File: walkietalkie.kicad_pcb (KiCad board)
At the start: 2 copper layers, 51.2 x 89.7 mm, 13 parts, among them J1 Conn_01x05_Pin, J2 Conn_01x02_Pin, J3 Conn_01x02_Pin, SW1 PTT, U2 NRF24L01_Breakout, U7 ER_OLEDM0.91_1x-I2C

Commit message: routing done
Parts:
- removed REF**: TestPoint_Pad_D1.0mm, TestPoint:TestPoint_Pad_D1.0mm
- added C1: C_Polarized, Capacitor_THT:CP_Radial_D8.0mm_P3.80mm, B.Cu at (133.0, 95.7)
- added R1: R, Resistor_THT:R_Axial_DIN0207_L6.3mm_D2.5mm_P10.16mm_Horizontal, F.Cu at (164.1, 76.0)
- added U6: SK12D07VG4, pcbcupidd_footprint:SK12D07VG4, B.Cu at (159.2, 147.2)
- D1: value LED_KRGB -> LED; footprint LED_THT:LED_D5.0mm-4_RGB -> LED_THT:LED_D5.0mm
- moved J2 24.3 mm to (150.1, 97.9)
- moved J3 24.3 mm to (156.1, 100.4)
- moved D1 2.83 mm to (159.3, 63.5)
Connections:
- BT1 pad 1: (no net) -> Net-(BT1-Pad1)
- BT1 pad 2: (no net) -> GND
- D1 pad 1: unconnected-(D1-K-Pad1) -> GND
- D1 pad 2: unconnected-(D1-RA-Pad2) -> Net-(D1-A)
- J1 pad 4: +3.3V -> +3V3
- J2 pad 1: unconnected-(J2-Pin_1-Pad1) -> /_RN
- J2 pad 2: unconnected-(J2-Pin_2-Pad2) -> /_RP
- J3 pad 1: unconnected-(J3-Pin_1-Pad1) -> /_LN
- J3 pad 2: unconnected-(J3-Pin_2-Pad2) -> /_LP
- U1 pad 14: unconnected-(U1-3V3-Pad14) -> +3V3
- U1 pad 16: unconnected-(U1-GND-Pad16) -> GND
- U1 pad 5: unconnected-(U1-A6-Pad5) -> /PTT
- U1 pad 6: /PTT -> /ENC_B
- U1 pad 8: /ENC_B -> /ENC_SW
- U1 pad 9: /ENC_SW -> /LED
- U2 pad 2: +3.3V -> +3V3
- U3 pad 10: unconnected-(U3-LP-Pad10) -> /_LP
- U3 pad 11: unconnected-(U3-LN-Pad11) -> /_LN
- U3 pad 12: unconnected-(U3-RN-Pad12) -> /_RN
- U3 pad 13: unconnected-(U3-RP-Pad13) -> /_RP
- U4 pad 5: +3.3V -> +3V3
- U5 pad 1: unconnected-(U5-3.3V-Pad1) -> +3V3
- U5 pad 8: unconnected-(U5-GND-Pad8) -> GND
- U7 pad 2: +3.3V -> +3V3
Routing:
- net +3V3: track 0.00 -> 165.7 mm, vias 0 -> 6
- net /LED: track 0.00 -> 90.6 mm
- net /ENC_B: track 88.8 -> 0.00 mm
- net /BAT: track 0.00 -> 36.6 mm
- net /_LP: track 0.00 -> 15.0 mm
- net /_LN: track 0.00 -> 15.0 mm
- net /_RN: track 0.00 -> 14.4 mm
- net /_RP: track 0.00 -> 14.4 mm
- net Net-(BT1-Pad1): track 0.00 -> 10.6 mm
- net Net-(D1-A): track 0.00 -> 3.24 mm
- net /PTT: track 89.2 -> 92.4 mm
- net /SCL: track 92.3 -> 93.6 mm
- net /SCK: track 37.3 -> 38.3 mm
- net /ENC_SW: track 87.4 -> 86.6 mm
- net /SDA: track 94.3 -> 93.7 mm
- added copper zone on B.Cu, net GND
- added copper zone on F.Cu, net GND

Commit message: feat: routing done
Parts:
- added G***: LOGO, LOGO, F.Cu at (134.7, 75.4)
- added G***: LOGO, LOGO, B.Cu at (134.7, 69.4)
- added G***: LOGO, LOGO, B.Cu at (127.0, 136.6)
- added G***: LOGO, LOGO, B.Cu at (134.8, 84.6)
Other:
- board text added: "47uf"
- board text added: "B+"
- board text added: "B-"
- board text added: "BATTERY HOLDER"
- board text added: "NRF24lo1+"
- board text added: "POWERED BY GLYPH"
- board text added: "SPEAKER 4OHM 3W"
- board text added: "TeleVox"
- board text added: "shop.pcbcupid.com"

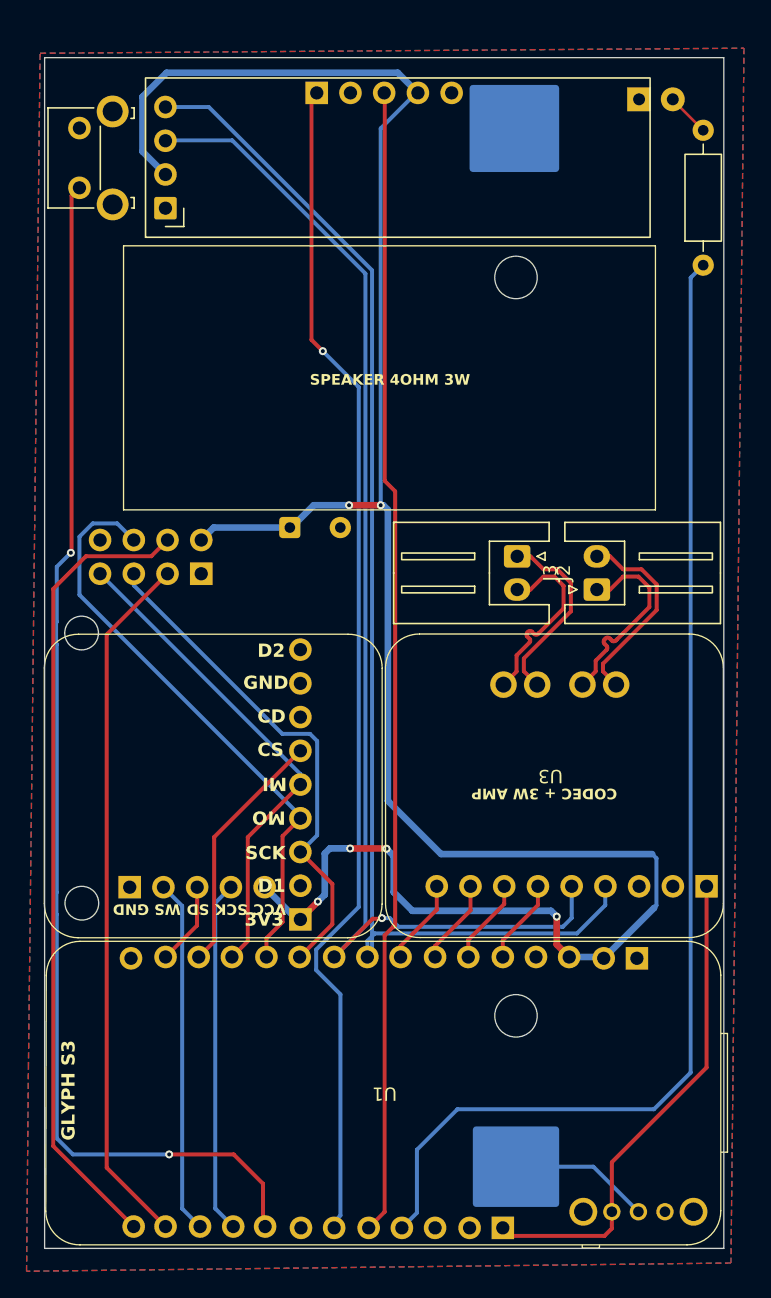
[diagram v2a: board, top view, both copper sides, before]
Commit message: feat: silkscreen done, gerber generated, sent to manufacturing
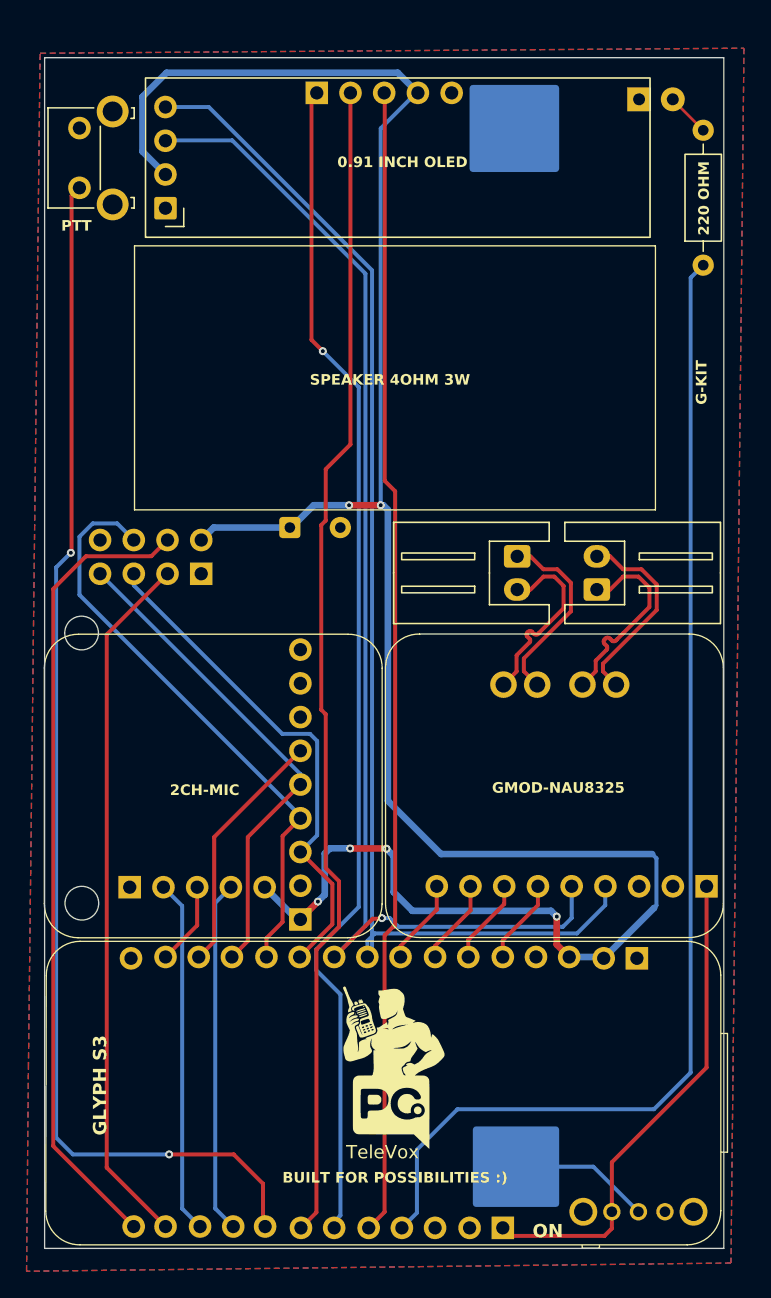
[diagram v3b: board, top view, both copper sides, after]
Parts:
- added G***: LOGO, LOGO, F.Cu at (140.6, 133.7)
- added G***: LOGO, LOGO, B.Cu at (140.6, 139.7)
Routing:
- net /ENC_B: track 0.00 -> 88.1 mm
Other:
- board text added: "+"
- board text added: "-"
- board text added: "0.91 INCH OLED"
- board text added: "220 OHM"
- board text added: "2CH-MIC"
- board text added: "BUILT FOR POSSIBILITIES :)"
- board text added: "Designed by ManIron"
- board text added: "G-KIT"
- board text added: "ON"
- board text added: "PTT"
- board text added: "ROTARY ENCODER"
